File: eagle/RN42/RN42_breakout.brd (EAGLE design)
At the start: 38.8 x 20.8 mm, 15 parts

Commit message: Update RN42 breakout board.
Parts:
- added L2, L3: (no value), led:CHIPLED_0603
- added R6, R7: 1k, rcl:R0603
- added SJ1, SJ2, SJ3, SJ4: (no value), jumper:SJ
- T1: value N-CHANNEL-MOSFET-BSS138 -> N-MOSFET
- moved R5 2.54 mm to (35.3, 16.3)
- moved C2 1.70 mm to (35.8, 5.84), turned to 270 degrees
- moved C3 0.76 mm to (23.1, 4.57)
- moved FACTORY_RST 0.76 mm to (12.2, 14.7)
- renumbered U$3 to T2, U$4 to T1
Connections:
- removed net LINK: U$1.15, U$1.16
- new net AUTODISCOVERY: SJ3.1, U$1.20
- new net BD_RATE: SJ4.1, U$1.4
- new net BT_MASTER: SJ1.1, U$1.3
- new net CTS: J1.3, U$1.16
- new net N$3: L2.A, R6.2
- new net N$4: L3.A, R7.1
- new net RTS: J1.4, U$1.15
- net 3V3: now also R7.2, SJ1.2, SJ3.2, SJ4.2
- net GND: now also J1.1, L2.C, L3.C, SJ2.2; no longer J1.3, U$1.4
- net RESET: now also SJ2.1; no longer J1.1
- net STATUS: now also R6.1; no longer J1.4
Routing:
- net CTS: track 0.00 -> 30.1 mm, vias 0 -> 1
- net RTS: track 0.00 -> 26.3 mm, vias 0 -> 1
- net STATUS: track 30.1 -> 4.24 mm, vias 2 -> 0
- net 3V3: track 53.3 -> 77.3 mm
- net RESET: track 30.7 -> 8.52 mm
- net BT_MASTER: track 0.00 -> 8.37 mm, vias 0 -> 1
- net AUTODISCOVERY: track 0.00 -> 7.55 mm, vias 0 -> 1
- net N$3: track 0.00 -> 7.37 mm
- net TX: track 20.2 -> 13.3 mm
- net BD_RATE: track 0.00 -> 6.73 mm, vias 0 -> 1
- net N$4: track 0.00 -> 1.45 mm
- net N$2: track 19.9 -> 21.3 mm, vias 0 -> 2
- net LINK: track 1.20 -> 0.00 mm
- net TXH: track 17.5 -> 16.4 mm
- net FACTORY_RST: track 6.65 -> 5.89 mm
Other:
- board size 38.8 x 20.8 mm -> 38.8 x 22.1 mm
- board text added: "3V3"
- board text added: "CTS"
- board text added: "PWR"
- board text added: "RTS"
- board text removed: "3.3V"
- board text removed: "STA"
- board text removed: "nRST"

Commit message: Pratically completed layout for RN42 breakout.
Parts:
- removed U$2: LM3480IM4, SparkFun-PowerIC:SOT23-3
- added SJ5: (no value), jumper:SJ
- added T3: LM3480IM4, SparkFun-PowerIC:SOT23-3
- R1: value (none) -> 1k
- R2, R3, R4, R5: value (none) -> 4.7k
- T2: value N-CHANNEL-MOSFET-BSS138 -> N-MOSFET
- moved U$1 5.58 mm to (11.7, 11.2)
- moved L1 5.58 mm to (23.4, 11.2)
- moved R1 5.58 mm to (23.4, 15.5)
- moved R2 5.58 mm to (23.6, 19.3)
- moved R4 5.58 mm to (18.0, 20.1)
- moved R6 5.58 mm to (14.2, 20.3)
- moved SJ3 5.58 mm to (11.4, 15.5)
- moved T1 5.58 mm to (26.9, 16.0)
- moved C1 5.58 mm to (23.4, 6.86)
- moved C2 5.58 mm to (31.0, 3.05)
- moved C3 5.58 mm to (18.3, 1.78)
- moved FACTORY_RST 5.58 mm to (7.37, 11.9)
- moved J1 5.58 mm to (36.6, 3.30)
- moved SJ2 5.58 mm to (12.7, 7.87)
- moved SJ4 5.58 mm to (8.38, 7.87)
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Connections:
- net 3V3: now also T3.1; no longer U$2.1
- net CTS: now also SJ5.2
- net GND: now also T3.3; no longer U$2.3
- net RTS: now also SJ5.1
- net VCC: now also T3.2; no longer U$2.2
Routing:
- net CTS: track 30.1 -> 31.1 mm
- net RTS: track 26.3 -> 27.2 mm
- net 3V3: track 77.3 -> 77.5 mm, vias 3 -> 4
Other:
- board size 38.8 x 22.1 mm -> 38.8 x 22.9 mm

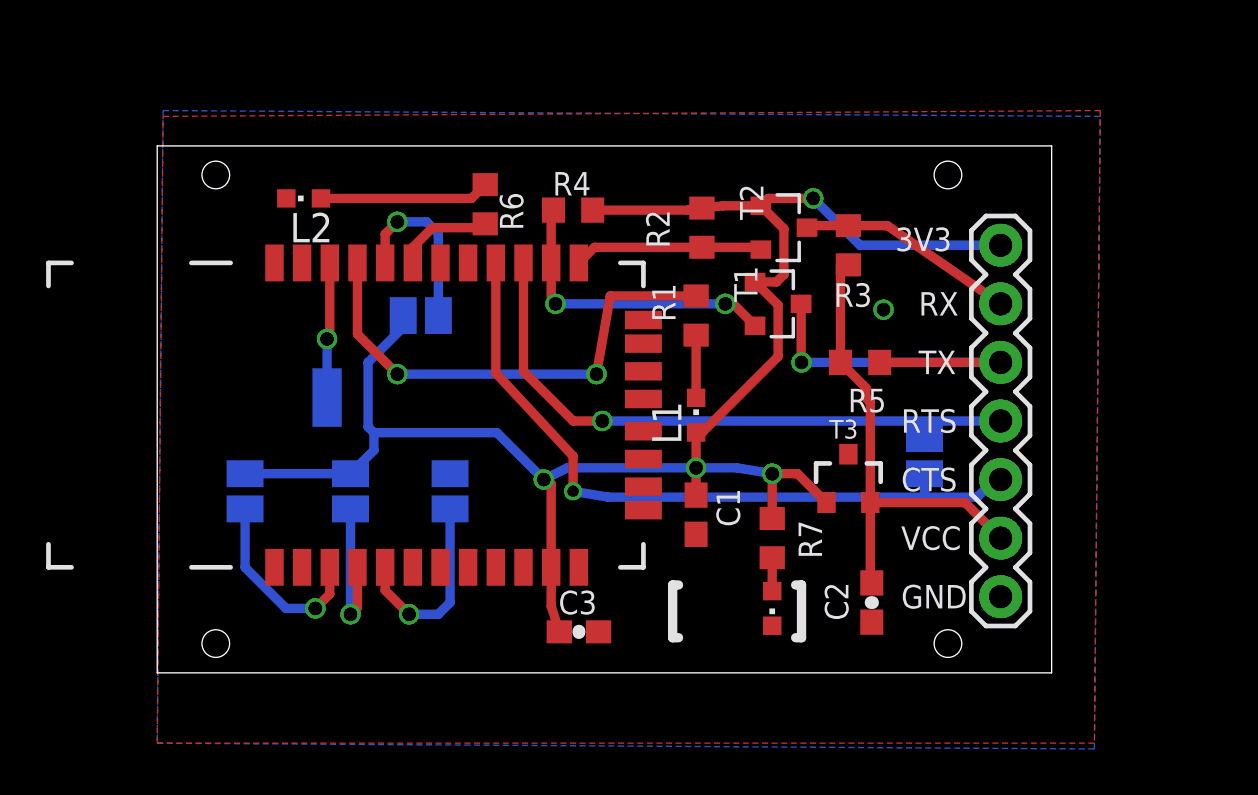
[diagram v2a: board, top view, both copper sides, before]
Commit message: Fix some labels on RN42 breakout.
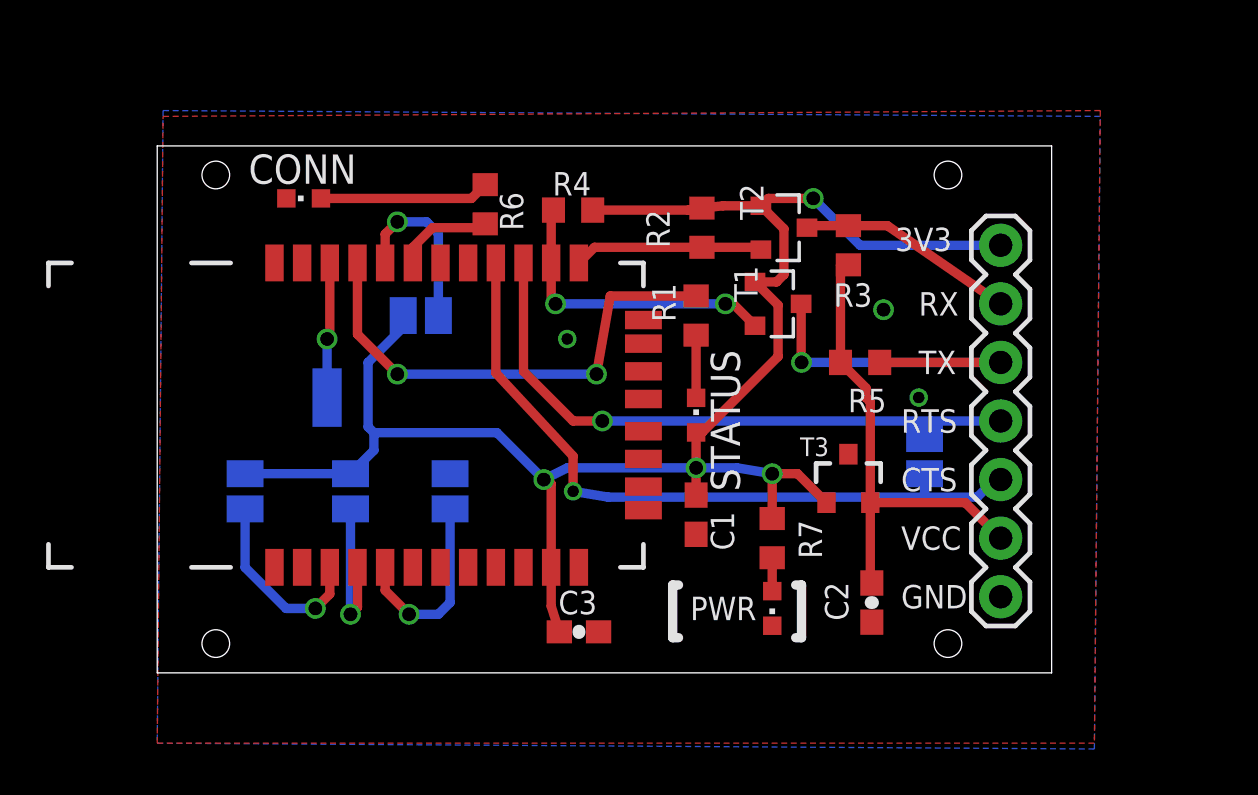
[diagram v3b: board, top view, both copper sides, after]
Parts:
- renumbered L1 to STATUS, L2 to CONN, SJ1 to MASTER, SJ2 to POWER, SJ3 to AUTODISCOVERY, SJ4 to BAUD

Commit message: Complete first release
Add production file.
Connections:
- net CTS: no longer J1.3
- net GND: now also J1.3; no longer J1.1
- net RTS: no longer J1.4
- net VCC: now also J1.4; no longer J1.2
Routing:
- net CTS: track 31.1 -> 27.5 mm
- net RTS: track 27.2 -> 24.1 mm
- net VCC: track 21.0 -> 21.8 mm
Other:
- board text removed: "CTS"
- board text removed: "RTS"
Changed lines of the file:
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@@
 <layer number="28" name="bValues" color="7" fill="1" visible="no" active="yes"/>
 <layer number="29" name="tStop" color="7" fill="3" visible="yes" active="yes"/>
-<layer number="30" name="bStop" color="7" fill="6" visible="yes" active="yes"/>
+<layer number="30" name="bStop" color="7" fill="6" visible="no" active="yes"/>
 <layer number="31" name="tCream" color="7" fill="4" visible="yes" active="yes"/>
-<layer number="32" name="bCream" color="7" fill="5" visible="yes" active="yes"/>
+<layer number="32" name="bCream" color="7" fill="5" visible="no" active="yes"/>
 <layer number="33" name="tFinish" color="6" fill="3" visible="no" active="yes"/>
 <layer number="34" name="bFinish" color="6" fill="6" visible="no" active="yes"/>
@@
 <layer number="42" name="bRestrict" color="1" fill="10" visible="no" active="yes"/>
 <layer number="43" name="vRestrict" color="2" fill="10" visible="no" active="yes"/>
-<layer number="44" name="Drills" color="7" fill="1" visible="yes" active="yes"/>
-<layer number="45" name="Holes" color="7" fill="1" visible="yes" active="yes"/>
-<layer number="46" name="Milling" color="3" fill="1" visible="yes" active="yes"/>
+<layer number="44" name="Drills" color="7" fill="1" visible="no" active="yes"/>
+<layer number="45" name="Holes" color="7" fill="1" visible="no" active="yes"/>
+<layer number="46" name="Milling" color="3" fill="1" visible="no" active="yes"/>
 <layer number="47" name="Measures" color="7" fill="1" visible="no" active="yes"/>
 <layer number="48" name="Document" color="7" fill="1" visible="no" active="yes"/>
@@
 <text x="33.02" y="12.954" size="1.016" layer="21" ratio="16">TX</text>
 <text x="33.02" y="15.494" size="1.016" layer="21" font="vector" ratio="16">RX</text>
-<text x="32.258" y="2.794" size="1.016" layer="21" font="vector" ratio="16">GND</text>
+<text x="32.258" y="10.414" size="1.016" layer="21" font="vector" ratio="16">GND</text>
 <text x="32.004" y="18.288" size="1.016" layer="21" font="vector" ratio="16">3V3</text>
 <text x="23.114" y="2.286" size="1.016" layer="25" font="vector" ratio="16">PWR</text>
-<text x="32.258" y="5.334" size="1.016" layer="21" font="vector" ratio="16">VCC</text>
+<text x="32.258" y="7.874" size="1.016" layer="21" font="vector" ratio="16">VCC</text>
 <wire x1="22.606" y1="3.81" x2="22.352" y2="3.81" width="0.4064" layer="21"/>
 <wire x1="22.352" y1="3.81" x2="22.352" y2="1.524" width="0.4064" layer="21"/>
@@
 <wire x1="27.94" y1="1.524" x2="27.94" y2="3.81" width="0.4064" layer="21"/>
 <wire x1="27.94" y1="3.81" x2="27.686" y2="3.81" width="0.4064" layer="21"/>
-<text x="32.258" y="7.874" size="1.016" layer="21" font="vector" ratio="16">CTS</text>
-<text x="32.258" y="10.414" size="1.016" layer="21" font="vector" ratio="16">RTS</text>
 <hole x="2.54" y="21.59" drill="1.2"/>
 <hole x="2.54" y="1.27" drill="1.2"/>
@@
 <elements>
 <element name="R1" library="rcl" package="R0603" value="1k" x="23.368" y="15.494" smashed="yes" rot="R270">
-<attribute name="NAME" x="21.463" y="16.891" size="1.016" layer="25" font="vector" ratio="16" rot="R270"/>
+<attribute name="NAME" x="21.463" y="17.907" size="1.016" layer="25" font="vector" ratio="16" rot="R270"/>
 <attribute name="VALUE" x="21.463" y="16.129" size="1.27" layer="27" rot="R270"/>
 </element>
@@
 <attribute name="OTHER" value="" x="27.178" y="19.304" size="1.778" layer="27" rot="R270" display="off"/>
 <attribute name="DIGIKEY" value="BSS138TR-ND" x="27.178" y="19.304" size="1.778" layer="27" rot="R270" display="off"/>
-<attribute name="NAME" x="25.273" y="21.209" size="1.016" layer="25" font="vector" ratio="16" rot="R270"/>
+<attribute name="NAME" x="25.527" y="22.733" size="1.016" layer="25" font="vector" ratio="16" rot="R270"/>
 </element>
 <element name="R2" library="rcl" package="R0603" value="4.7k" x="23.622" y="19.304" smashed="yes" rot="R90">
@@
 <attribute name="OTHER" value="" x="26.924" y="16.002" size="1.778" layer="27" rot="R270" display="off"/>
 <attribute name="DIGIKEY" value="BSS138TR-ND" x="26.924" y="16.002" size="1.778" layer="27" rot="R270" display="off"/>
-<attribute name="NAME" x="25.019" y="17.653" size="1.016" layer="25" font="vector" ratio="16" rot="R270"/>
+<attribute name="NAME" x="26.035" y="14.351" size="1.016" layer="25" font="vector" ratio="16" rot="R270"/>
 </element>
 <element name="R4" library="rcl" package="R0603" value="4.7k" x="18.034" y="20.066" smashed="yes">
@@
 </element>
 <element name="MASTER" library="jumper" package="SJ" value="" x="3.81" y="7.874" smashed="yes" rot="MR90">
-<attribute name="NAME" x="5.461" y="4.445" size="1.27" layer="26" font="vector" ratio="16" rot="MR90"/>
+<attribute name="NAME" x="5.207" y="4.445" size="1.27" layer="26" font="vector" ratio="16" rot="MR90"/>
 <attribute name="VALUE" x="3.81" y="8.2741" size="0.02" layer="28" rot="MR90"/>
 </element>
@@
 <contactref element="L3" pad="C"/>
 <via x="31.496" y="15.748" extent="1-16" drill="0.6" shape="square"/>
-<contactref element="J1" pad="1"/>
+<contactref element="J1" pad="3"/>
 <contactref element="POWER" pad="2"/>
 <via x="17.78" y="14.478" extent="1-16" drill="0.5" diameter="0.3048" shape="octagon"/>
@@
 <wire x1="15.884" y1="17.776" x2="15.884" y2="13.072" width="0.4064" layer="1"/>
 <via x="19.304" y="10.922" extent="1-16" drill="0.6" shape="square"/>
-<contactref element="J1" pad="4"/>
 <wire x1="19.304" y1="10.922" x2="33.528" y2="10.922" width="0.4064" layer="16"/>
-<wire x1="33.528" y1="10.922" x2="36.576" y2="10.922" width="0.4064" layer="16"/>
 <wire x1="15.884" y1="13.072" x2="18.034" y2="10.922" width="0.4064" layer="1"/>
 <wire x1="18.034" y1="10.922" x2="19.304" y2="10.922" width="0.4064" layer="1"/>
@@
 <wire x1="30.734" y1="11.938" x2="30.734" y2="12.358" width="0.4064" layer="1"/>
 <wire x1="30.734" y1="12.358" x2="29.63" y2="13.462" width="0.4064" layer="1"/>
-<contactref element="J1" pad="2"/>
-<wire x1="30.922" y1="7.382" x2="35.036" y2="7.382" width="0.4064" layer="1"/>
-<wire x1="35.036" y1="7.382" x2="36.576" y2="5.842" width="0.4064" layer="1"/>
+<contactref element="J1" pad="4"/>
 <wire x1="30.922" y1="7.382" x2="30.922" y2="3.964" width="0.4064" layer="1"/>
 <wire x1="30.922" y1="3.964" x2="30.988" y2="3.898" width="0.4064" layer="1"/>
+<wire x1="36.576" y1="10.922" x2="34.462" y2="10.922" width="0.4064" layer="1"/>
+<wire x1="34.462" y1="10.922" x2="30.922" y2="7.382" width="0.4064" layer="1"/>
 </signal>
 <signal name="3V3">
@@
 <wire x1="18.034" y1="9.398" x2="18.034" y2="7.874" width="0.4064" layer="1"/>
 <via x="18.034" y="7.874" extent="1-16" drill="0.5"/>
-<contactref element="J1" pad="3"/>
 <wire x1="18.034" y1="7.874" x2="19.558" y2="7.62" width="0.4064" layer="16"/>
 <wire x1="19.558" y1="7.62" x2="33.274" y2="7.62" width="0.4064" layer="16"/>
-<wire x1="33.274" y1="7.62" x2="35.56" y2="7.62" width="0.4064" layer="16"/>
-<wire x1="35.56" y1="7.62" x2="36.322" y2="8.382" width="0.4064" layer="16"/>
-<wire x1="36.322" y1="8.382" x2="36.576" y2="8.382" width="0.4064" layer="16"/>
 <contactref element="SJ5" pad="2"/>
 <wire x1="33.274" y1="8.636" x2="33.274" y2="7.62" width="0.4064" layer="16"/>
